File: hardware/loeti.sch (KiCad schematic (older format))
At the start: 55 parts, among them J1 USB_C_Receptacle_USB2.0, J2 Samtec FTS-107-01-L-D, J3 AudioJack4, Q1 BC817, Q2 BC817, Q3 BC807, Q4 Si4825DDY, DMG4435SSS, IRF939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, SW1 key2, SW2 SW_SPST, SW3 SW_SPST, U1 AP2204R-3.3, U2 STUSB4500QTR, U3 USBLC6-2SC6, U4 EA_DOGS104B-A, U5 STM32F042K6Tx, U6 ADS1118IDGS

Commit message: improved UI
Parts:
- added R15: 10m, Resistor_SMD:R_2010_5025Metric_Pad1.52x2.65mm_HandSolder, symbol Device:R
- added R16: 1k, Resistor_SMD:R_0603_1608Metric_Pad1.05x0.95mm_HandSolder, symbol Device:R
- added U7: INA138, Package_TO_SOT_SMD:SOT-23-5, symbol Amplifier_Current:INA138
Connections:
- net ADC_IN2: now also R16.1, U7.1; no longer TP1.1
- net GND: now also R16.2, U7.2 (GND)
- net VBUS: now also R15.1, U7.3 (+), U7.5 (V+); no longer Q4.1 (S), Q4.2 (S), Q4.3 (S)
- new net POT: TP1.1
- new net SHUNT-: Q4.1 (S), Q4.2 (S), Q4.3 (S), R15.2, U7.4 (-)
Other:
- moved on the sheet: J3
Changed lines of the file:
@@
 Wire Wire Line
 	6750 3850 6750 4000
-Text GLabel 14100 7000 2    50   Input ~ 0
-HEATER+
+Text GLabel 12400 8850 2    50   Input ~ 0
+SHUNT-
 Wire Wire Line
 	12500 1700 12500 2000
@@
 Text GLabel 11600 4950 0    50   Input ~ 0
 T-
-Text GLabel 14300 750  0    50   Input ~ 0
+Text GLabel 15250 8250 0    50   Input ~ 0
 HEATER-
-Text GLabel 14300 950  0    50   Input ~ 0
+Text GLabel 15250 8450 0    50   Input ~ 0
 T+
-Text GLabel 14300 1050 0    50   Input ~ 0
+Text GLabel 15250 8550 0    50   Input ~ 0
 HEATER+
-Text GLabel 14300 850  0    50   Input ~ 0
+Text GLabel 15250 8350 0    50   Input ~ 0
 T-
 $Comp
 L Connector:AudioJack4 J3
 U 1 1 5E93DE18
-P 14500 850
-F 0 "J3" H 14170 825 50  0000 R CNN
-F 1 "AudioJack4" H 14170 734 50  0000 R CNN
-F 2 "custom:CUI_SJ-43614-SMT" H 14500 850 50  0001 C CNN
-F 3 "~" H 14500 850 50  0001 C CNN
-	1    14500 850
+P 15450 8350
+F 0 "J3" H 15120 8325 50  0000 R CNN
+F 1 "AudioJack4" H 15120 8234 50  0000 R CNN
+F 2 "custom:CUI_SJ-43614-SMT" H 15450 8350 50  0001 C CNN
+F 3 "~" H 15450 8350 50  0001 C CNN
+	1    15450 8350
 	-1   0    0    -1
 $EndComp
@@
 ADC_IN2
 Text GLabel 8850 2550 2    50   Input ~ 0
-POT
+CUR
 Wire Wire Line
 	8750 2550 8850 2550
@@
 Wire Wire Line
 	15100 6650 15100 6700
-Wire Wire Line
-	13200 6150 13200 6550
 $Comp
 L power:VBUS #PWR?
@@
 Text Notes 5150 1550 0    79   ~ 0
 MCU and programming header
+$Comp
+L Amplifier_Current:INA138 U7
+U 1 1 5EAFC52B
+P 11650 8550
+F 0 "U7" H 11994 8596 50  0000 L CNN
+F 1 "INA138" H 11994 8505 50  0000 L CNN
+F 2 "Package_TO_SOT_SMD:SOT-23-5" H 11650 8550 50  0001 C CNN
+F 3 "http://www.ti.com/lit/ds/symlink/ina138.pdf" H 11650 8555 50  0001 C CNN
+	1    11650 8550
+	-1   0    0    -1
+$EndComp
+Wire Wire Line
+	11950 8450 12150 8450
+Wire Wire Line
+	11950 8650 12150 8650
+Wire Wire Line
+	12400 8850 12300 8850
+Text GLabel 13300 6350 2    50   Input ~ 0
+SHUNT+
+Text GLabel 12400 8250 2    50   Input ~ 0
+SHUNT+
+Text GLabel 13300 6500 2    50   Input ~ 0
+SHUNT-
+Text GLabel 14100 7000 2    50   Input ~ 0
+HEATER+
+Wire Wire Line
+	12400 8250 12300 8250
+$Comp
+L power:GND #PWR0103
+U 1 1 5EBF5E66
+P 11750 8850
+F 0 "#PWR0103" H 11750 8600 50  0001 C CNN
+F 1 "GND" H 11755 8677 50  0000 C CNN
+F 2 "" H 11750 8850 50  0001 C CNN
+F 3 "" H 11750 8850 50  0001 C CNN
+	1    11750 8850
+	1    0    0    -1
+$EndComp
+$Comp
+L Device:R R16
+U 1 1 5EBF6918
+P 10850 8750
+F 0 "R16" H 10919 8796 50  0000 L CNN
+F 1 "1k" H 10919 8705 50  0000 L CNN
+F 2 "Resistor_SMD:R_0603_1608Metric_Pad1.05x0.95mm_HandSolder" V 10780 8750 50  0001 C CNN
+F 3 "~" H 10850 8750 50  0001 C CNN
+	1    10850 8750
+	1    0    0    -1
+$EndComp
+$Comp
+L power:GND #PWR0104
+U 1 1 5EBF727C
+P 10850 8900
+F 0 "#PWR0104" H 10850 8650 50  0001 C CNN
+F 1 "GND" H 10855 8727 50  0000 C CNN
+F 2 "" H 10850 8900 50  0001 C CNN
+F 3 "" H 10850 8900 50  0001 C CNN
+	1    10850 8900
+	1    0    0    -1
+$EndComp
+Wire Wire Line
+	11350 8550 10850 8550
+Wire Wire Line
+	10850 8550 10850 8600
+$Comp
+L power:VBUS #PWR?
+U 1 1 5EC012C6
+P 11750 8250
+AR Path="/588FA5F7/5EC012C6" Ref="#PWR?"  Part="1"
+AR Path="/588FD270/5EC012C6" Ref="#PWR?"  Part="1"
+AR Path="/5EC012C6" Ref="#PWR0105"  Part="1"
+F 0 "#PWR0105" H 11750 8100 50  0001 C CNN
+F 1 "VBUS" H 11765 8423 50  0000 C CNN
+F 2 "" H 11750 8250 50  0001 C CNN
+F 3 "" H 11750 8250 50  0001 C CNN
+	1    11750 8250
+	1    0    0    -1
+$EndComp
+Text GLabel 10750 8550 0    50   Input ~ 0
+CUR
+Wire Wire Line
+	10850 8550 10750 8550
+Connection ~ 10850 8550
+$Comp
+L Device:R R15
+U 1 1 5EC172DA
+P 12300 8550
+F 0 "R15" H 12369 8596 50  0000 L CNN
+F 1 "10m" H 12369 8505 50  0000 L CNN
+F 2 "Resistor_SMD:R_2010_5025Metric_Pad1.52x2.65mm_HandSolder" V 12230 8550 50  0001 C CNN
+F 3 "~" H 12300 8550 50  0001 C CNN
+	1    12300 8550
+	1    0    0    -1
+$EndComp
+Wire Wire Line
+	12300 8250 12300 8400
+Wire Wire Line
+	12300 8700 12300 8850
+Wire Wire Line
+	12150 8450 12150 8250
+Wire Wire Line
+	12150 8250 12300 8250
+Connection ~ 12300 8250
+Wire Wire Line
+	12150 8650 12150 8850
+Wire Wire Line
+	12150 8850 12300 8850
+Connection ~ 12300 8850
+Wire Wire Line
+	13200 6150 13200 6350
+Wire Wire Line
+	13200 6350 13300 6350
+Wire Wire Line
+	13300 6500 13200 6500
+Wire Wire Line
+	13200 6500 13200 6550
 $EndSCHEMATC

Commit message: cold junction compensation v3 hardware
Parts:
- removed TP1: WIPE, TestPoint:TestPoint_THTPad_4.0x4.0mm_Drill2.0mm, symbol Connector:TestPoint
- added C18, C19: 0.1μF, Capacitor_SMD:C_0603_1608Metric_Pad1.05x0.95mm_HandSolder, symbol Device:C
- added R17: 10k, Resistor_SMD:R_0603_1608Metric_Pad1.05x0.95mm_HandSolder, symbol Device:R
- added R18, R19: 1k, Resistor_SMD:R_0603_1608Metric_Pad1.05x0.95mm_HandSolder, symbol Device:R
- added U8: OPA340NA, Package_TO_SOT_SMD:SOT-23-5, symbol Amplifier_Operational:OPA340NA
- R15: value 10m -> WSL2010R0200FEA18
- R16: value 1k -> 100k
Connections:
- net +3V3: now also U7.5 (V+), C19.2, U8.5 (V+)
- net ADC_IN2: now also C18.1, R19.2; no longer R16.1, U7.1
- net GND: now also C18.2, C19.1, R18.1, U8.2 (V-)
- net VBUS: now also R17.2; no longer U7.5 (V+)
- net ADC_IN7: now reaches U5.13 (PA7)
- net ADC_IN7: now also R17.1, R18.2
- new net: R16.1, U7.1, U8.3 (+)
- new net: R19.1, U8.1, U8.4 (-)
- no-connect marks 20 -> 19
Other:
- note added: "1.6 kHz low-pass"
- note added: "Connectors and test points"
- note added: "Current measurement"
- note added: "USB and power"
- moved on the sheet: C1, C2, C3, C4, C5, C6, D1, D2, J1, J3, R1, R15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

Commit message: final?
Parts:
- R10, R11: value 470 -> 47
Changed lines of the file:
@@
 P 11900 4950
 F 0 "R11" H 11830 4904 50  0000 R CNN
-F 1 "470" H 11830 4995 50  0000 R CNN
+F 1 "47" H 11830 4995 50  0000 R CNN
 F 2 "Resistor_SMD:R_0603_1608Metric_Pad1.05x0.95mm_HandSolder" V 11830 4950 50  0001 C CNN
 F 3 "~" H 11900 4950 50  0001 C CNN
@@
 P 11900 4450
 F 0 "R10" H 11830 4404 50  0000 R CNN
-F 1 "470" H 11830 4495 50  0000 R CNN
+F 1 "47" H 11830 4495 50  0000 R CNN
 F 2 "Resistor_SMD:R_0603_1608Metric_Pad1.05x0.95mm_HandSolder" V 11830 4450 50  0001 C CNN
 F 3 "~" H 11900 4450 50  0001 C CNN

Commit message: updates to schematic
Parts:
- R19: value 1k -> 10k
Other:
- note added: "159 Hz low-pass"
- note added: "1690 Hz low Pass"
- note removed: "1.6 kHz low-pass"
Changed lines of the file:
@@
 P 11300 9000
 F 0 "R19" H 11369 9046 50  0000 L CNN
-F 1 "1k" H 11369 8955 50  0000 L CNN
+F 1 "10k" H 11369 8955 50  0000 L CNN
 F 2 "Resistor_SMD:R_0603_1608Metric_Pad1.05x0.95mm_HandSolder" V 11230 9000 50  0001 C CNN
 F 3 "~" H 11300 9000 50  0001 C CNN
@@
 $EndComp
 Text Notes 10700 8900 0    50   ~ 0
-1.6 kHz low-pass
+159 Hz low-pass
 Wire Notes Line
 	10250 7850 15900 7850
@@
 Text GLabel 4300 4200 2    50   Input ~ 0
 VOLT
+Text Notes 11300 4800 0    50   ~ 0
+1690 Hz low Pass
 $EndSCHEMATC

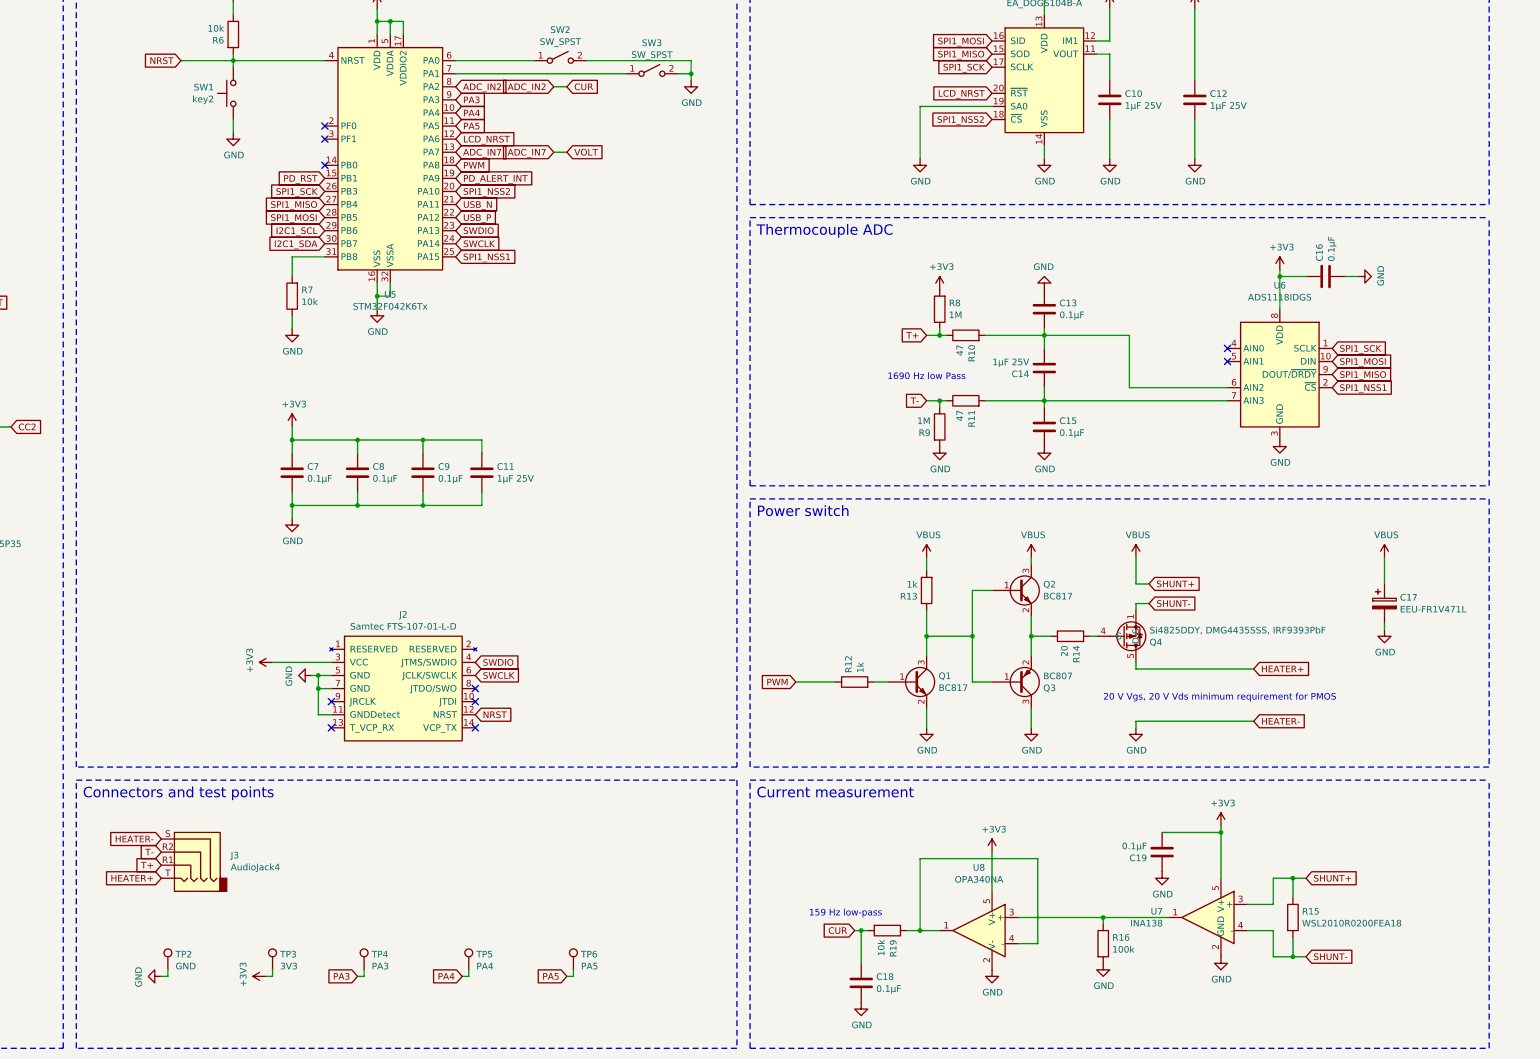
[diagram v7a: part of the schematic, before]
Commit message: Switched to chibios 20.3.1
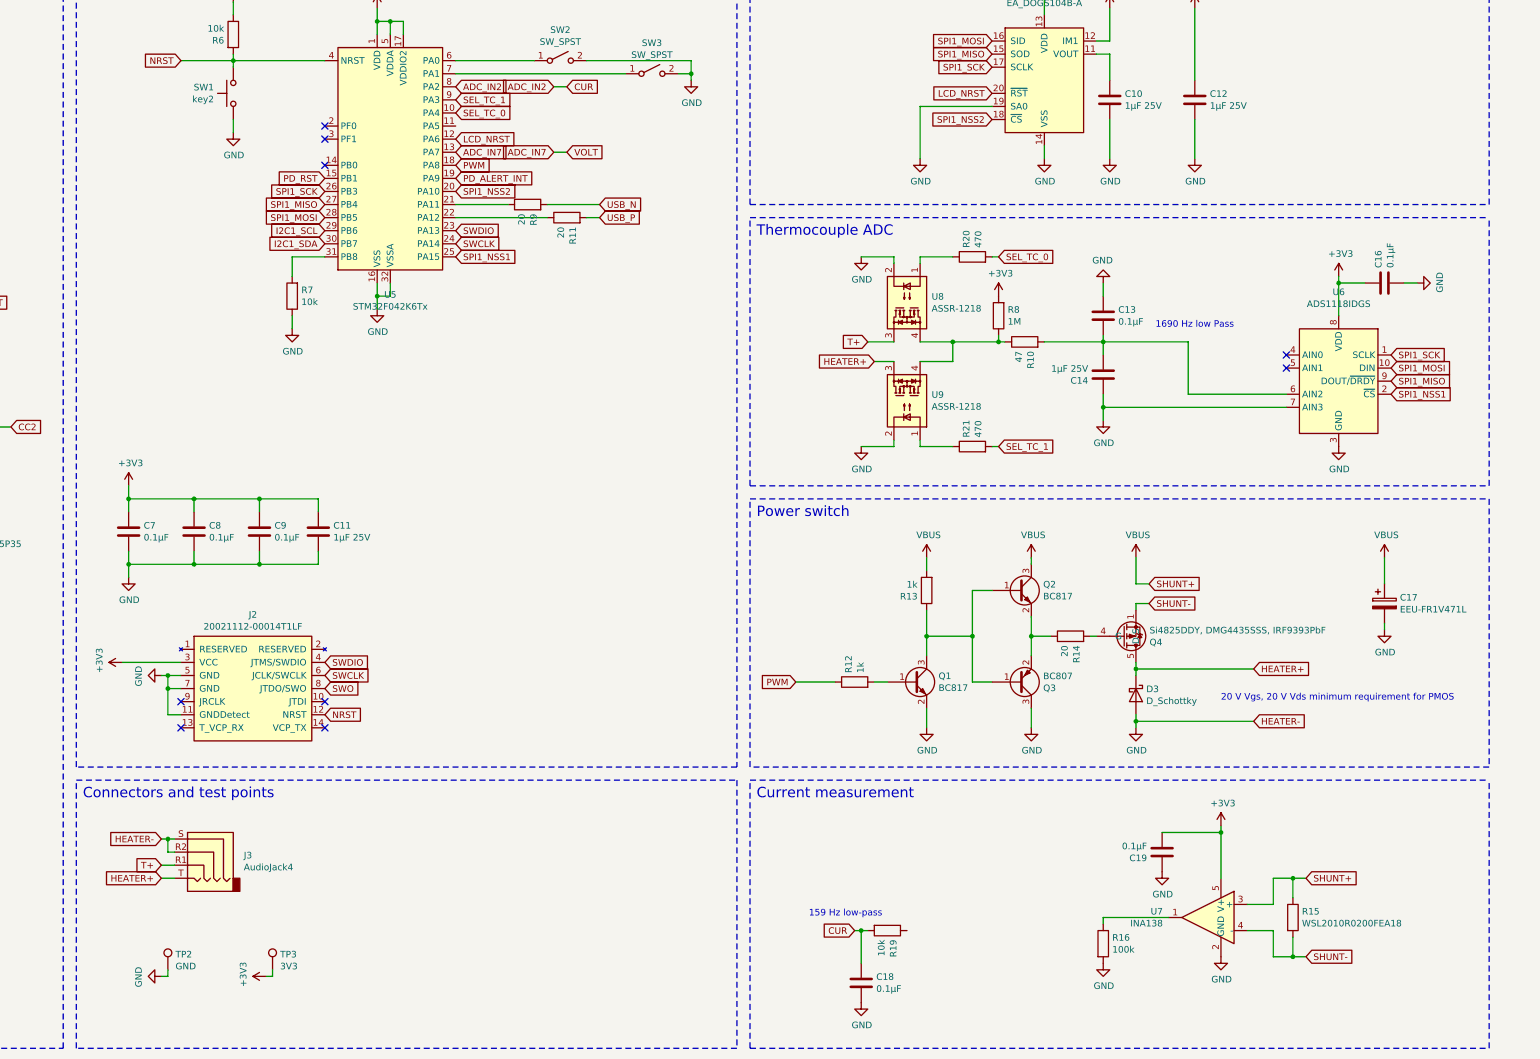
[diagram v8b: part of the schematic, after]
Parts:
- removed C15: 0.1μF, Capacitor_SMD:C_0603_1608Metric_Pad1.05x0.95mm_HandSolder, symbol Device:C
- removed TP4: PA3, TestPoint:TestPoint_THTPad_2.0x2.0mm_Drill1.0mm, symbol Connector:TestPoint
- removed TP5: PA4, TestPoint:TestPoint_THTPad_2.0x2.0mm_Drill1.0mm, symbol Connector:TestPoint
- removed TP6: PA5, TestPoint:TestPoint_THTPad_2.0x2.0mm_Drill1.0mm, symbol Connector:TestPoint
- removed U8: OPA340NA, Package_TO_SOT_SMD:SOT-23-5, symbol Amplifier_Operational:OPA340NA
- added D3: D_Schottky, Diode_SMD:D_SOD-123, symbol Device:D_Schottky
- added R20, R21: 470, Resistor_SMD:R_0603_1608Metric_Pad1.05x0.95mm_HandSolder, symbol Device:R
- added U8, U9: ASSR-1218, Package_SO:SO-4_4.4x4.3mm_P2.54mm, symbol Relay_SolidState:ASSR-1218
- J2: value Samtec FTS-107-01-L-D -> 20021112-00014T1LF; footprint Connector_PinHeader_1.27mm:PinHeader_2x07_P1.27mm_Vertical -> Connector_PinHeader_1.27mm:PinHeader_2x07_P1.27mm_Horizontal
- R11: value 47 -> 20
- R9: value 1M -> 20
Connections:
- net GND: now also C14.1, J3.R2, U6.7 (AIN3), D3.2 (A), U8.2, U9.2; no longer R9.2
- net HEATER+: now also D3.1 (K), U9.3
- net T+: now also U8.3; no longer R10.1, R8.1
- net USB_N: now also R9.2; no longer U5.21 (PA11)
- net USB_P: now also R11.2; no longer U5.22 (PA12)
- net SWO: now reaches J2.8 (JTDO/SWO)
- net PA3 renamed SEL_TC_1
- net SEL_TC_1: now also R21.2
- net PA4 renamed SEL_TC_0
- net SEL_TC_0: now also R20.2
- net PA5: no longer names the net of U5.11 (PA5)
- removed net T-: J3.R2, R11.1, R9.1
- new net: R10.1, R8.1, U8.4, U9.4
- new net: R9.1, U5.21 (PA11)
- new net: R11.1, U5.22 (PA12)
- new net: R20.1, U8.1
- new net: R21.1, U9.1
- no-connect marks 19 -> 18
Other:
- moved on the sheet: C11, C13, C14, C16, C7, C8, C9, J2, J3, R10, R8, U6
